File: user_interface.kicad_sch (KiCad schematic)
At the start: 29 parts, among them J3 Внутр. коннектор потенциометр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, J4 Внутр. коннектор галлетника (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, SW1 Кнопка тактовая 6x6 без фикса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, SW2 Кнопка тактовая 6x6 без фикса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, SW3 Кнопка тактовая 6x6 без фикса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, SW4 Кнопка тактовая 6x6 без фикса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, SW5 Кнопка тактовая 6x6 без фикса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, SW6 Кнопка тактовая 6x6 без фикса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

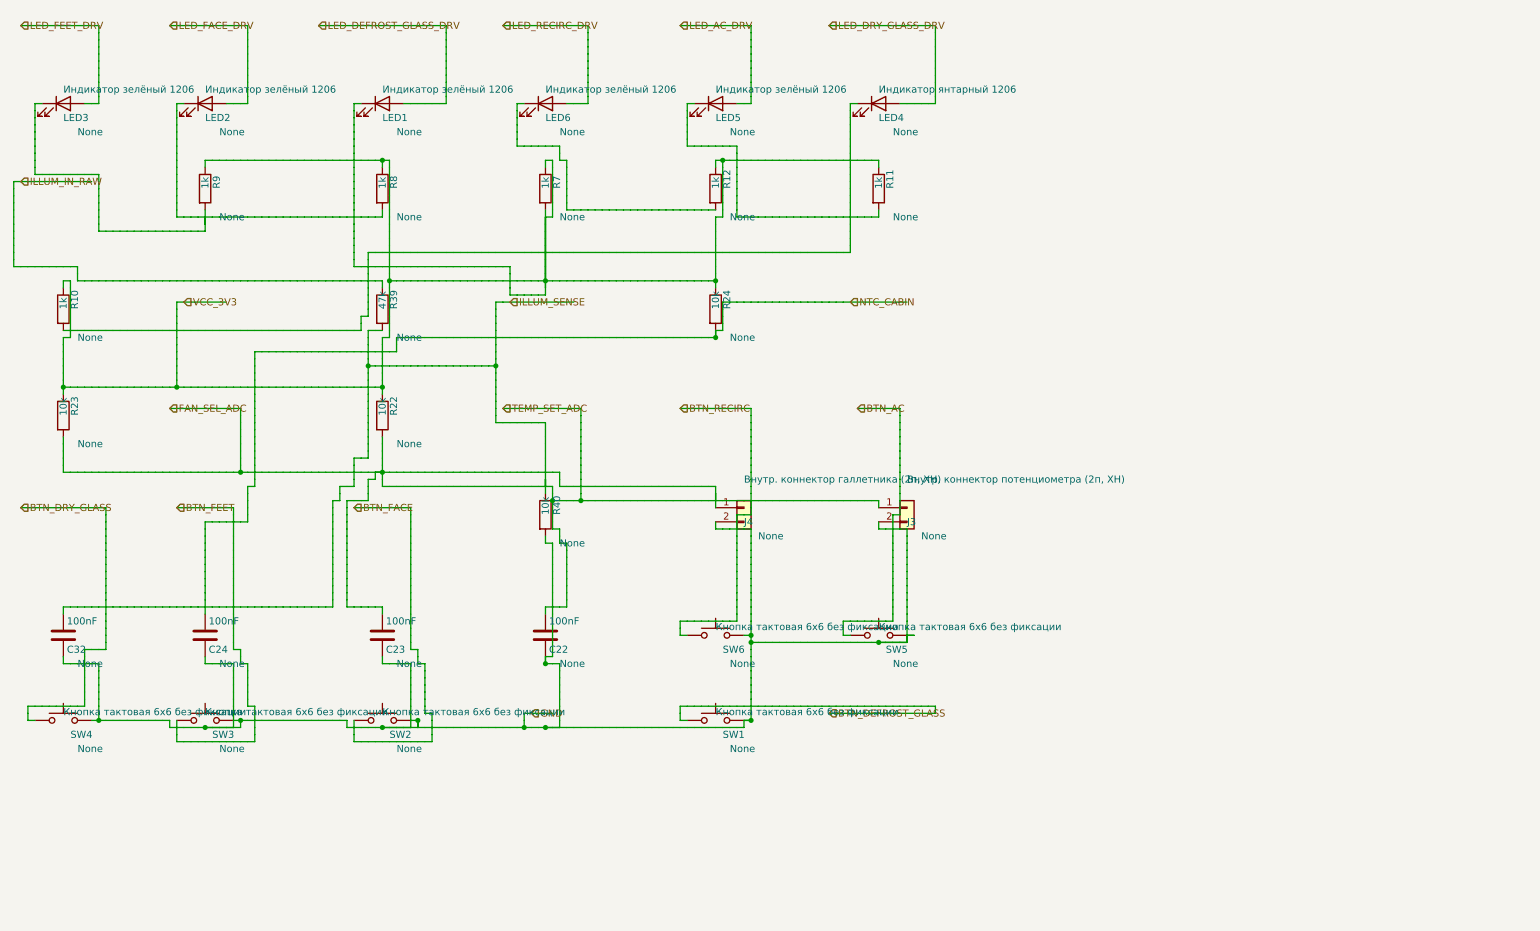
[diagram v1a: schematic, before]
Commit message: fix router map cell no more mark for pins
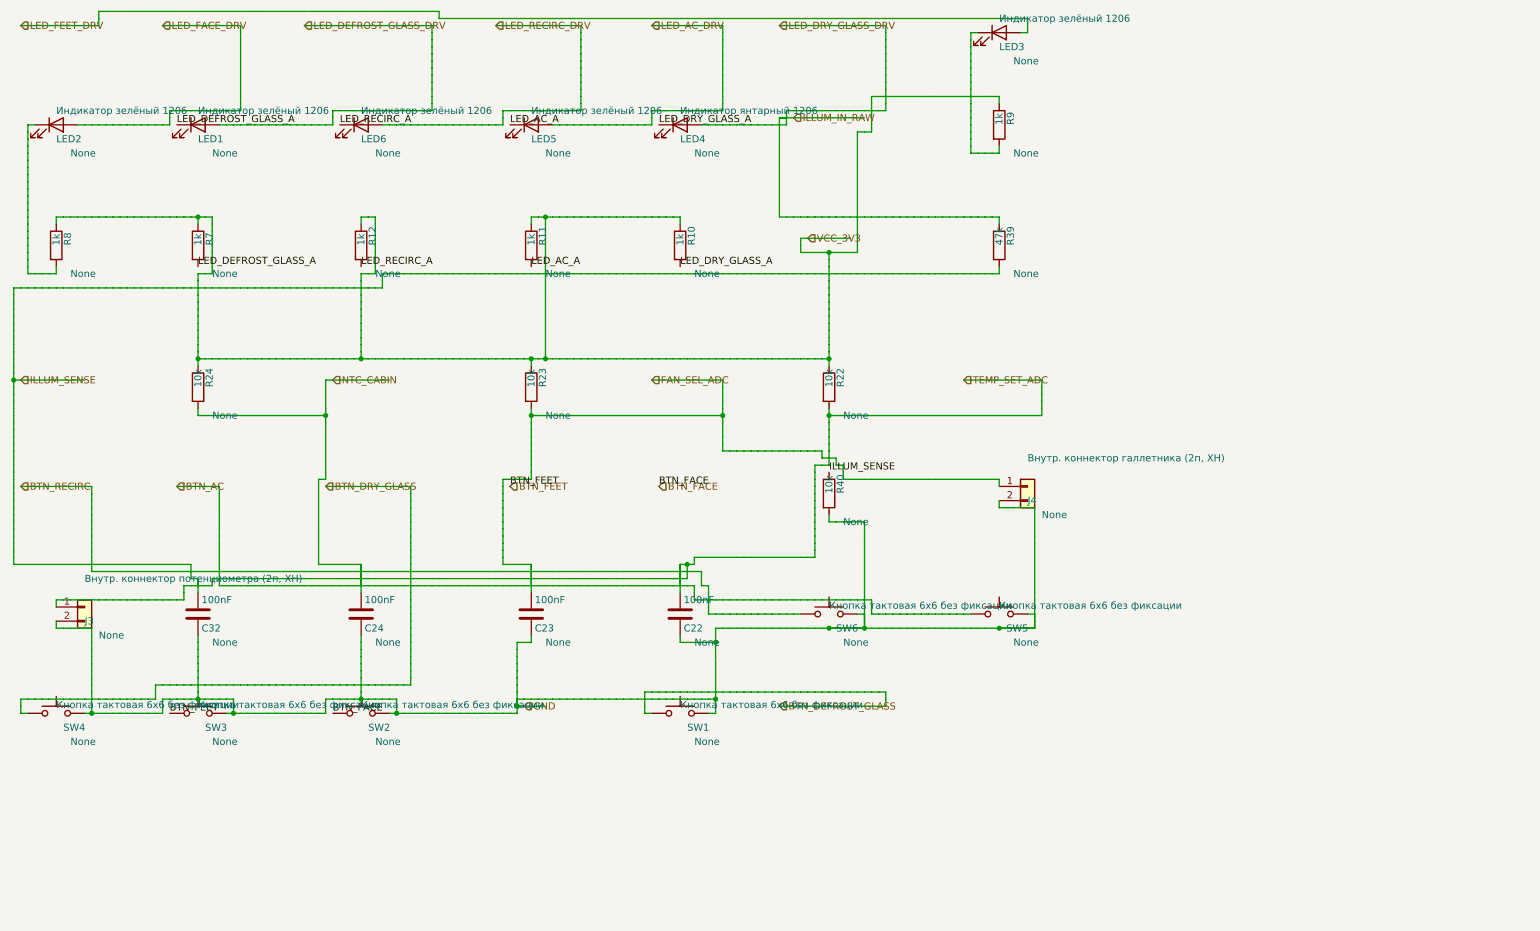
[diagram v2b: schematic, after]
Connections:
- net LED_DRY_GLASS_DRV is gone; now on net BTN_AC: LED4.2 (A)
- net BTN_AC: no longer LED1.1 (K), LED2.1 (K), LED4.1 (K), LED5.1 (K), R10.2, R11.2, R7.2, R8.2, SW2.1, SW3.1
- net LED_RECIRC_A: now reaches LED6.1 (K), R12.2
- new net: LED2.1 (K), R8.2
- new net BTN_FACE: SW2.1
- new net BTN_FEET: SW3.1
- new net LED_AC_A: LED5.1 (K), R11.2
- new net LED_DEFROST_GLASS_A: LED1.1 (K), R7.2
- new net LED_DRY_GLASS_A: LED4.1 (K), R10.2

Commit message: рефакторинг проекта и начала прогона тестов
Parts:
- removed J4: Внутр. коннектор галлетника (2п, XH), symbol Connector_Generic:Conn_01x02
- added J4: Внутр. коннектор галлетника (5п, XH), symbol Connector_Generic:Conn_01x05
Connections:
- net LED_DEFROST_GLASS_A is gone; now on net BTN_AC: LED1.1 (K), R7.2
- net LED_DRY_GLASS_A is gone; now on net BTN_AC: LED4.1 (K), R10.2
- net BTN_AC: now also LED2.1 (K), R8.2, J4.1 (Pin_1), J4.2 (Pin_2), J4.3 (Pin_3), J4.4 (Pin_4), J4.5 (Pin_5); no longer LED4.2 (A), SW4.1
- net LED_AC_A: no longer names the net of LED5.1 (K), R11.2
- net LED_RECIRC_A: no longer names the net of LED6.1 (K), R12.2
- new net BTN_DRY_GLASS: SW4.1
- new net LED_DRY_GLASS_DRV: LED4.2 (A)

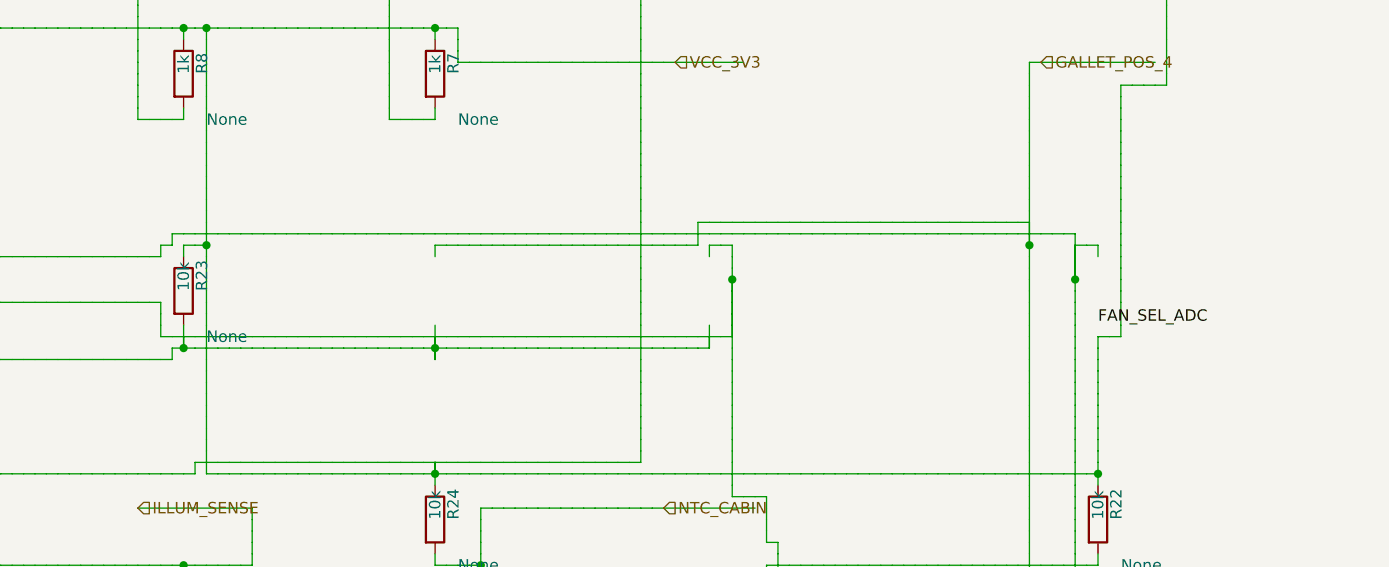
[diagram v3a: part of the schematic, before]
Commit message: исправлены метки
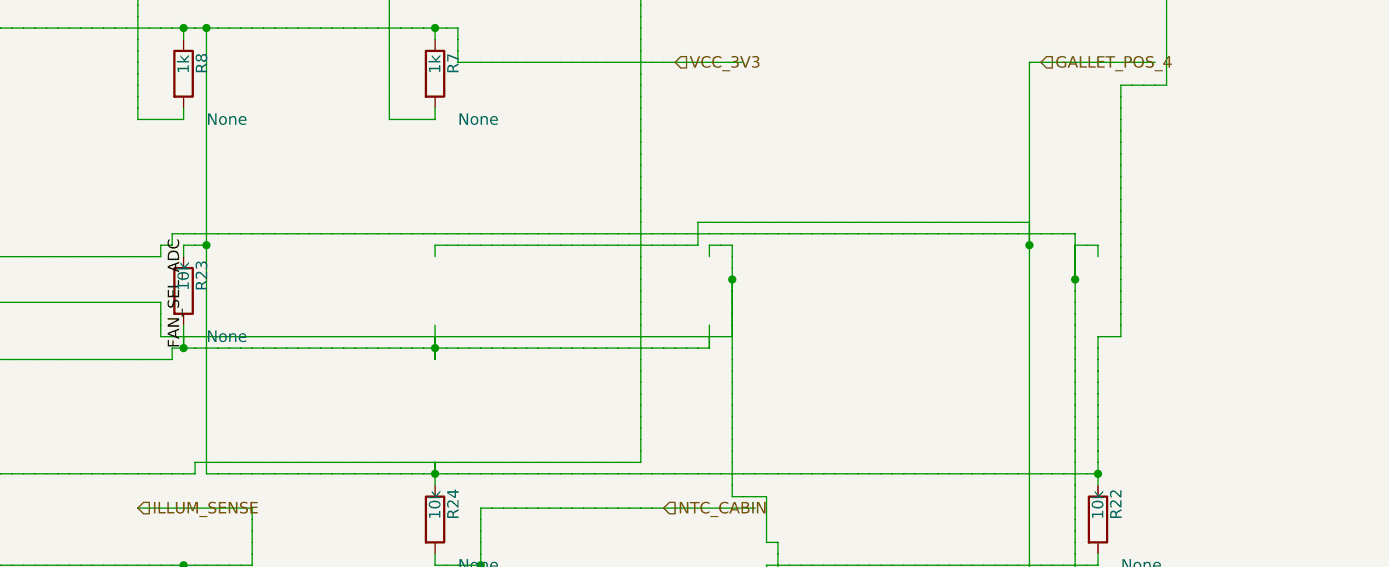
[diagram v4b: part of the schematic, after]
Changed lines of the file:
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@@
 		(instances
 			(project "Untitled"
-				(path "/8b66d29f-ae4d-40a4-99d0-003370dee9fa"
+				(path "/8a0a7786-a70b-4b2c-981e-9e6dc655a95c"
 					(reference "C22")
 					(unit 1)
@@
 		(instances
 			(project "Untitled"
-				(path "/8b66d29f-ae4d-40a4-99d0-003370dee9fa"
+				(path "/8a0a7786-a70b-4b2c-981e-9e6dc655a95c"
 					(reference "C23")
 					(unit 1)
@@
 		(instances
 			(project "Untitled"
-				(path "/8b66d29f-ae4d-40a4-99d0-003370dee9fa"
+				(path "/8a0a7786-a70b-4b2c-981e-9e6dc655a95c"
 					(reference "C24")
 					(unit 1)
@@
 		(instances
 			(project "Untitled"
-				(path "/8b66d29f-ae4d-40a4-99d0-003370dee9fa"
+				(path "/8a0a7786-a70b-4b2c-981e-9e6dc655a95c"
 					(reference "C32")
 					(unit 1)
@@
 		(instances
 			(project "Untitled"
-				(path "/8b66d29f-ae4d-40a4-99d0-003370dee9fa"
+				(path "/8a0a7786-a70b-4b2c-981e-9e6dc655a95c"
 					(reference "J3")
 					(unit 1)
@@
 		(instances
 			(project "Untitled"
-				(path "/8b66d29f-ae4d-40a4-99d0-003370dee9fa"
+				(path "/8a0a7786-a70b-4b2c-981e-9e6dc655a95c"
 					(reference "J4")
 					(unit 1)
@@
 		(instances
 			(project "Untitled"
-				(path "/8b66d29f-ae4d-40a4-99d0-003370dee9fa"
+				(path "/8a0a7786-a70b-4b2c-981e-9e6dc655a95c"
 					(reference "LED1")
 					(unit 1)
@@
 		(instances
 			(project "Untitled"
-				(path "/8b66d29f-ae4d-40a4-99d0-003370dee9fa"
+				(path "/8a0a7786-a70b-4b2c-981e-9e6dc655a95c"
 					(reference "LED2")
 					(unit 1)
@@
 		(instances
 			(project "Untitled"
-				(path "/8b66d29f-ae4d-40a4-99d0-003370dee9fa"
+				(path "/8a0a7786-a70b-4b2c-981e-9e6dc655a95c"
 					(reference "LED3")
 					(unit 1)
@@
 		(instances
 			(project "Untitled"
-				(path "/8b66d29f-ae4d-40a4-99d0-003370dee9fa"
+				(path "/8a0a7786-a70b-4b2c-981e-9e6dc655a95c"
 					(reference "LED4")
 					(unit 1)
@@
 		(instances
 			(project "Untitled"
-				(path "/8b66d29f-ae4d-40a4-99d0-003370dee9fa"
+				(path "/8a0a7786-a70b-4b2c-981e-9e6dc655a95c"
 					(reference "LED5")
 					(unit 1)
@@
 		(instances
 			(project "Untitled"
-				(path "/8b66d29f-ae4d-40a4-99d0-003370dee9fa"
+				(path "/8a0a7786-a70b-4b2c-981e-9e6dc655a95c"
 					(reference "LED6")
 					(unit 1)
@@
 		(instances
 			(project "Untitled"
-				(path "/8b66d29f-ae4d-40a4-99d0-003370dee9fa"
+				(path "/8a0a7786-a70b-4b2c-981e-9e6dc655a95c"
 					(reference "R7")
 					(unit 1)
@@
 		(instances
 			(project "Untitled"
-				(path "/8b66d29f-ae4d-40a4-99d0-003370dee9fa"
+				(path "/8a0a7786-a70b-4b2c-981e-9e6dc655a95c"
 					(reference "R8")
 					(unit 1)
@@
 		(instances
 			(project "Untitled"
-				(path "/8b66d29f-ae4d-40a4-99d0-003370dee9fa"
+				(path "/8a0a7786-a70b-4b2c-981e-9e6dc655a95c"
 					(reference "R9")
 					(unit 1)
@@
 		(instances
 			(project "Untitled"
-				(path "/8b66d29f-ae4d-40a4-99d0-003370dee9fa"
+				(path "/8a0a7786-a70b-4b2c-981e-9e6dc655a95c"
 					(reference "R10")
 					(unit 1)
@@
 		(instances
 			(project "Untitled"
-				(path "/8b66d29f-ae4d-40a4-99d0-003370dee9fa"
+				(path "/8a0a7786-a70b-4b2c-981e-9e6dc655a95c"
 					(reference "R11")
 					(unit 1)
@@
 		(instances
 			(project "Untitled"
-				(path "/8b66d29f-ae4d-40a4-99d0-003370dee9fa"
+				(path "/8a0a7786-a70b-4b2c-981e-9e6dc655a95c"
 					(reference "R12")
 					(unit 1)
@@
 		(instances
 			(project "Untitled"
-				(path "/8b66d29f-ae4d-40a4-99d0-003370dee9fa"
+				(path "/8a0a7786-a70b-4b2c-981e-9e6dc655a95c"
 					(reference "R22")
 					(unit 1)
@@
 		(instances
 			(project "Untitled"
-				(path "/8b66d29f-ae4d-40a4-99d0-003370dee9fa"
+				(path "/8a0a7786-a70b-4b2c-981e-9e6dc655a95c"
 					(reference "R23")
 					(unit 1)
@@
 		(instances
 			(project "Untitled"
-				(path "/8b66d29f-ae4d-40a4-99d0-003370dee9fa"
+				(path "/8a0a7786-a70b-4b2c-981e-9e6dc655a95c"
 					(reference "R24")
 					(unit 1)
@@
 		(instances
 			(project "Untitled"
-				(path "/8b66d29f-ae4d-40a4-99d0-003370dee9fa"
+				(path "/8a0a7786-a70b-4b2c-981e-9e6dc655a95c"
 					(reference "R39")
 					(unit 1)
@@
 		(instances
 			(project "Untitled"
-				(path "/8b66d29f-ae4d-40a4-99d0-003370dee9fa"
+				(path "/8a0a7786-a70b-4b2c-981e-9e6dc655a95c"
 					(reference "R40")
 					(unit 1)
@@
 		(instances
 			(project "Untitled"
-				(path "/8b66d29f-ae4d-40a4-99d0-003370dee9fa"
+				(path "/8a0a7786-a70b-4b2c-981e-9e6dc655a95c"
 					(reference "SW1")
 					(unit 1)
@@
 		(instances
 			(project "Untitled"
-				(path "/8b66d29f-ae4d-40a4-99d0-003370dee9fa"
+				(path "/8a0a7786-a70b-4b2c-981e-9e6dc655a95c"
 					(reference "SW2")
 					(unit 1)
@@
 		(instances
 			(project "Untitled"
-				(path "/8b66d29f-ae4d-40a4-99d0-003370dee9fa"
+				(path "/8a0a7786-a70b-4b2c-981e-9e6dc655a95c"
 					(reference "SW3")
 					(unit 1)
@@
 		(instances
 			(project "Untitled"
-				(path "/8b66d29f-ae4d-40a4-99d0-003370dee9fa"
+				(path "/8a0a7786-a70b-4b2c-981e-9e6dc655a95c"
 					(reference "SW4")
 					(unit 1)
@@
 		(instances
 			(project "Untitled"
-				(path "/8b66d29f-ae4d-40a4-99d0-003370dee9fa"
+				(path "/8a0a7786-a70b-4b2c-981e-9e6dc655a95c"
 					(reference "SW5")
 					(unit 1)
@@
 		(instances
 			(project "Untitled"
-				(path "/8b66d29f-ae4d-40a4-99d0-003370dee9fa"
+				(path "/8a0a7786-a70b-4b2c-981e-9e6dc655a95c"
 					(reference "SW6")
 					(unit 1)
@@
 	)
 	(label "BTN_FACE"
-		(at 97.79 157.48 0)
+		(at 97.79 157.48 180)
 		(effects
 			(font
@@
 	)
 	(label "BTN_FACE"
-		(at 157.48 113.03 0)
+		(at 157.48 113.03 0.0000)
 		(effects
 			(font
@@
 	)
 	(label "BTN_FEET"
-		(at 66.04 157.48 0)
+		(at 66.04 157.48 180)
 		(effects
 			(font
@@
 	)
 	(label "BTN_FEET"
-		(at 125.73 113.03 0)
+		(at 125.73 113.03 0.0000)
 		(effects
 			(font
@@
 	)
 	(label "BTN_DRY_GLASS"
-		(at 33.02 157.48 0)
+		(at 33.02 157.48 180)
 		(effects
 			(font
@@
 	)
 	(label "BTN_DRY_GLASS"
-		(at 96.52 113.03 0)
+		(at 96.52 113.03 0.0000)
 		(effects
 			(font
@@
 	)
 	(label "FAN_SEL_ADC"
-		(at 204.47 69.85 0)
+		(at 102.87 72.39 270)
 		(effects
 			(font

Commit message: fix writer
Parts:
- added R25: 20k, symbol Device:R
- added R26: 10k, symbol Device:R
- added R27: 4.7k, symbol Device:R
- added R28: 1k, symbol Device:R
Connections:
- net BTN_AC: no longer C22.1, C22.2, C23.1, C23.2, C24.1, C24.2, C32.1, C32.2, J3.1 (Pin_1), J3.2 (Pin_2), J4.1 (Pin_1), J4.2 (Pin_2), J4.3 (Pin_3), J4.4 (Pin_4), J4.5 (Pin_5), LED1.1 (K), LED2.1 (K), LED3.1 (K), LED4.1 (K), R10.1, R10.2, R11.1, R12.1, R22.1, R22.2, R23.1, R23.2, R24.1, R24.2, R39.1, R39.2, R40.1, R40.2, R7.1, R7.2, R8.1, R8.2, R9.1, R9.2, SW1.1, SW1.2, SW2.2, SW3.2, SW4.2, SW5.2, SW6.1, SW6.2
- new net: LED3.1 (K), R9.2
- new net: LED1.1 (K), R7.2
- new net: LED2.1 (K), R8.2
- new net: LED4.1 (K), R10.2
- new net BTN_DEFROST_GLASS: SW1.1
- new net BTN_RECIRC: SW6.1
- new net FAN_SEL_ADC: C23.1, R23.2, R25.2, R27.2, R28.2
- new net GALLET_POS_1: J4.2 (Pin_2), R25.1
- new net GALLET_POS_2: J4.3 (Pin_3), R26.1
- new net GALLET_POS_3: J4.4 (Pin_4), R27.1
- new net GALLET_POS_4: J4.5 (Pin_5), R28.1
- new net GND: C22.2, C23.2, C24.2, C32.2, J3.2 (Pin_2), J4.1 (Pin_1), R40.2, SW1.2, SW2.2, SW3.2, SW4.2, SW5.2, SW6.2
- new net ILLUM_IN_RAW: R39.1
- new net ILLUM_SENSE: C32.1, R39.2, R40.1
- new net NTC_CABIN: C24.1, R24.2
- new net TEMP_SET_ADC: C22.1, J3.1 (Pin_1), R22.2
- new net VCC_3V3: R10.1, R11.1, R12.1, R22.1, R23.1, R24.1, R7.1, R8.1, R9.1
